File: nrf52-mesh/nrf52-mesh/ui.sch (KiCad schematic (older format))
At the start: 3 parts

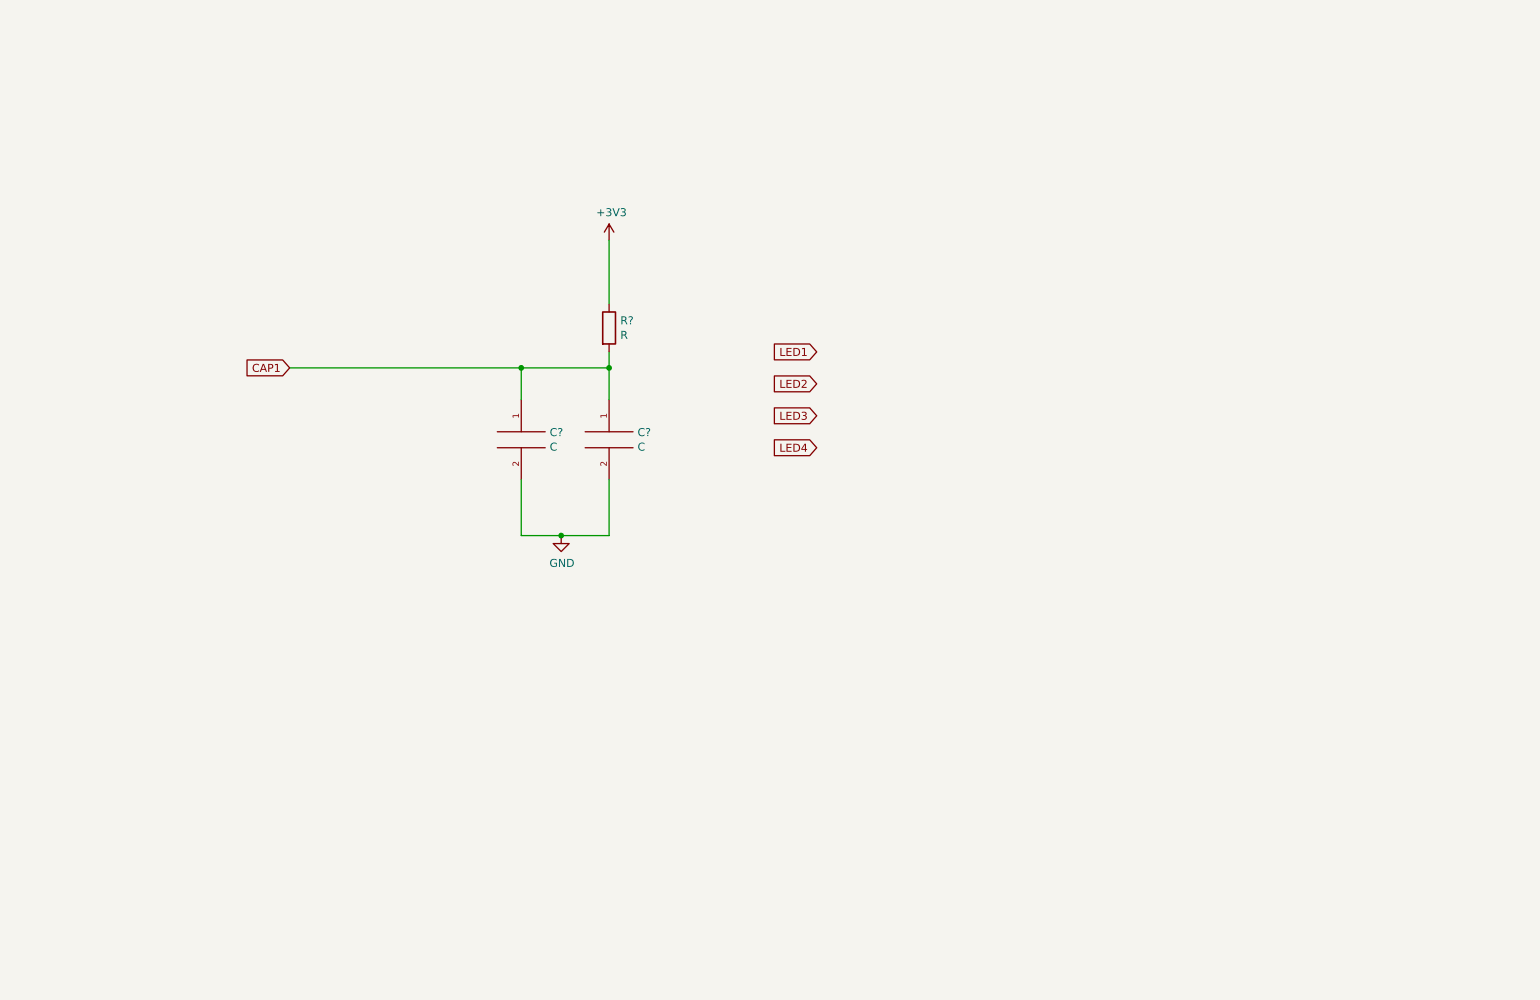
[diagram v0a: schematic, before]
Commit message: CP2102N + MAX1555 + FAN5341 + TPS560200 + TLV62568
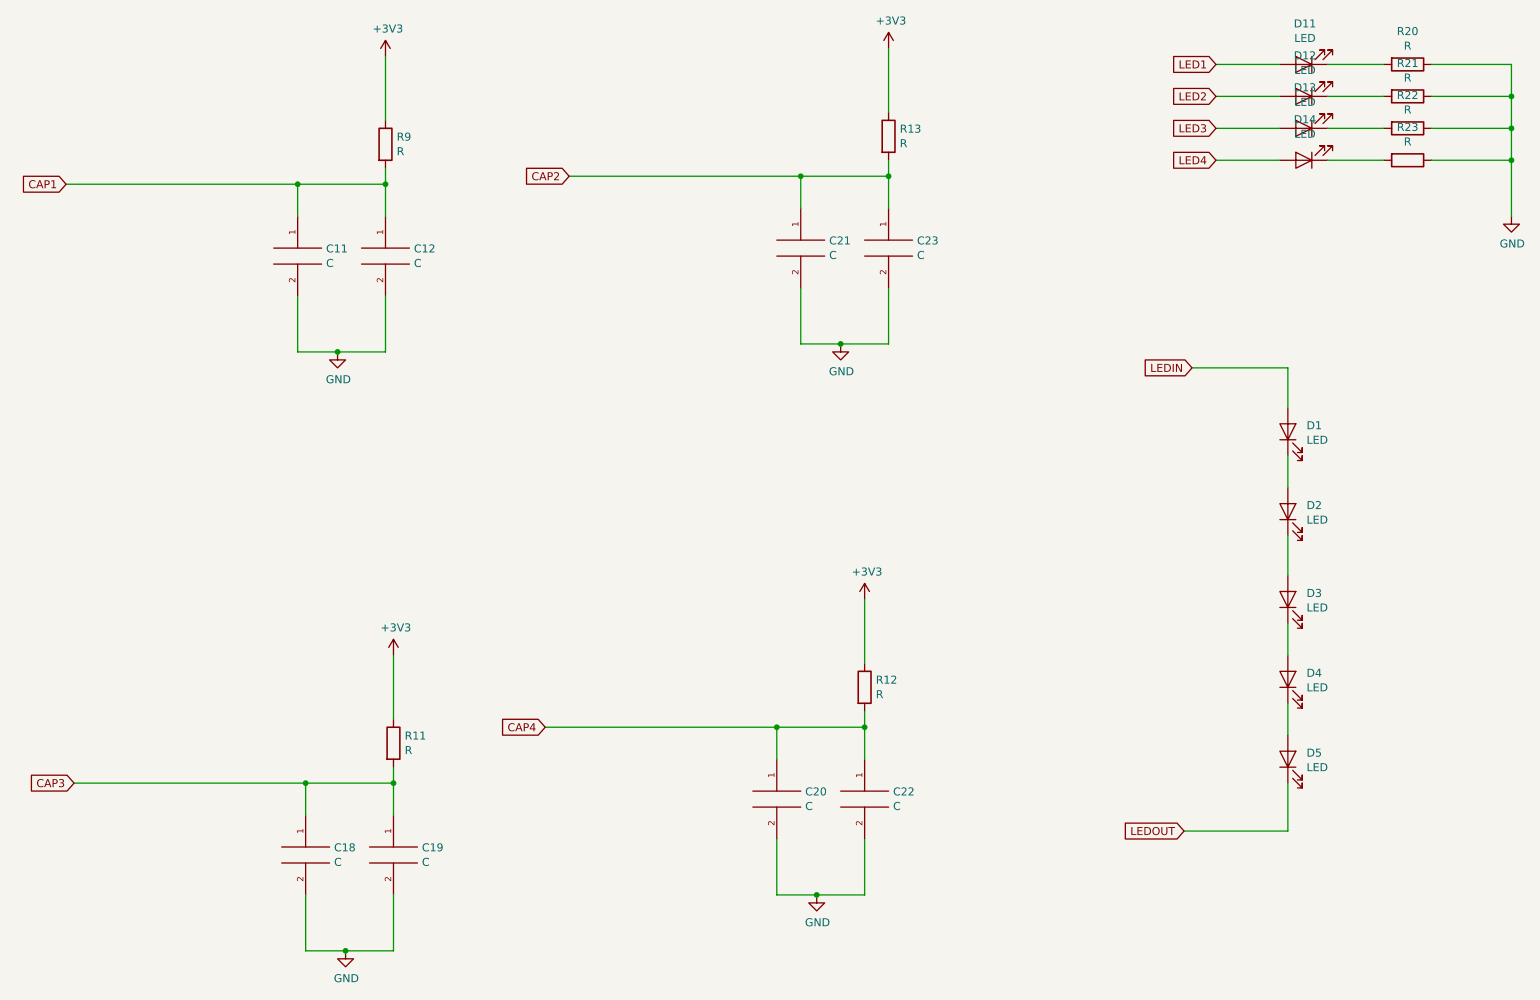
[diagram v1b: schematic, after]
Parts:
- added C18, C19, C20, C21, C22, C23: C, symbol pspice:C
- added D1, D11, D12, D13, D14, D2, D3, D4, D5: LED, symbol Device:LED
- added R11, R12, R13, R20, R21, R22, R23: R, symbol Device:R
- gave numbers to parts that had none: 3
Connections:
- net +3V3: now also R11.1, R12.1, R13.1
- net GND: now also C18.2, C19.2, C20.2, C21.2, C22.2, C23.2, R20.1, R21.1, R22.1, R23.1
- net LED1: now also D11.2 (A)
- net LED2: now also D12.2 (A)
- net LED3: now also D13.2 (A)
- net LED4: now also D14.2 (A)
- new net: D11.1 (K), R20.2
- new net: D12.1 (K), R21.2
- new net: D13.1 (K), R22.2
- new net: D14.1 (K), R23.2
- new net: D2.1 (K), D3.2 (A)
- new net: D1.1 (K), D2.2 (A)
- new net: D3.1 (K), D4.2 (A)
- new net: D4.1 (K), D5.2 (A)
- new net CAP2: C21.1, C23.1, R13.2
- new net CAP3: C18.1, C19.1, R11.2
- new net CAP4: C20.1, C22.1, R12.2
- new net LEDIN: D1.2 (A)
- new net LEDOUT: D5.1 (K)
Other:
- moved on the sheet: C11, C12, R9

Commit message: CP2102N + MAX1555 + FAN5341 + TPS560200 + TLV62568
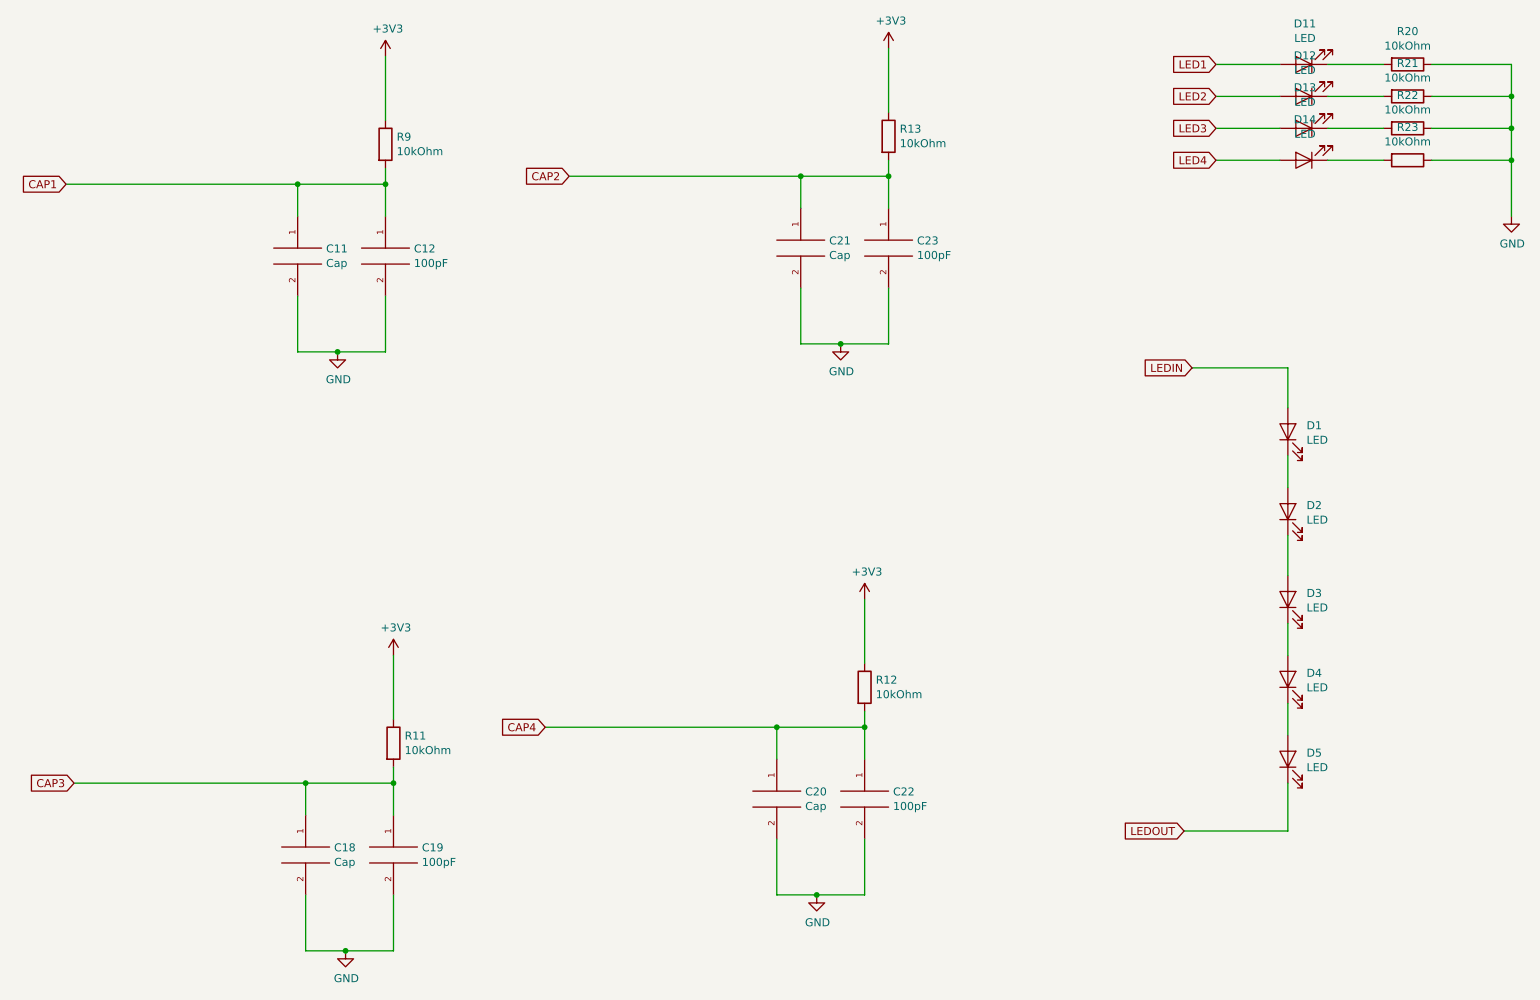
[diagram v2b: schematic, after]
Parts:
- C11, C18, C20, C21: value C -> Cap; footprint (none) -> kifootp:CAPBUTTON
- C12, C19, C22, C23: value C -> 100pF; footprint (none) -> Capacitor_SMD:C_0402_1005Metric
- D1, D11, D12, D13, D14, D2, D3, D4, D5: footprint (none) -> LED_SMD:LED_1206_3216Metric
- R11, R12, R13, R20, R21, R22, R23, R9: value R -> 10kOhm; footprint (none) -> Resistor_SMD:R_0402_1005Metric
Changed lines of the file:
@@
 P 3250 2400
 F 0 "C12" H 3428 2446 50  0000 L CNN
-F 1 "C" H 3428 2355 50  0000 L CNN
-F 2 "" H 3250 2400 50  0001 C CNN
+F 1 "100pF" H 3428 2355 50  0000 L CNN
+F 2 "Capacitor_SMD:C_0402_1005Metric" H 3250 2400 50  0001 C CNN
 F 3 "~" H 3250 2400 50  0001 C CNN
 	1    3250 2400
@@
 P 2700 2400
 F 0 "C11" H 2878 2446 50  0000 L CNN
-F 1 "C" H 2878 2355 50  0000 L CNN
-F 2 "" H 2700 2400 50  0001 C CNN
+F 1 "Cap" H 2878 2355 50  0000 L CNN
+F 2 "kifootp:CAPBUTTON" H 2700 2400 50  0001 C CNN
 F 3 "~" H 2700 2400 50  0001 C CNN
 	1    2700 2400
@@
 P 3250 1700
 F 0 "R9" H 3320 1746 50  0000 L CNN
-F 1 "R" H 3320 1655 50  0000 L CNN
-F 2 "" V 3180 1700 50  0001 C CNN
+F 1 "10kOhm" H 3320 1655 50  0000 L CNN
+F 2 "Resistor_SMD:R_0402_1005Metric" V 3180 1700 50  0001 C CNN
 F 3 "~" H 3250 1700 50  0001 C CNN
 	1    3250 1700
@@
 F 0 "D11" H 8993 945 50  0000 C CNN
 F 1 "LED" H 8993 1036 50  0000 C CNN
-F 2 "" H 9000 1200 50  0001 C CNN
+F 2 "LED_SMD:LED_1206_3216Metric" H 9000 1200 50  0001 C CNN
 F 3 "~" H 9000 1200 50  0001 C CNN
 	1    9000 1200
@@
 F 0 "D12" H 8993 1145 50  0000 C CNN
 F 1 "LED" H 8993 1236 50  0000 C CNN
-F 2 "" H 9000 1400 50  0001 C CNN
+F 2 "LED_SMD:LED_1206_3216Metric" H 9000 1400 50  0001 C CNN
 F 3 "~" H 9000 1400 50  0001 C CNN
 	1    9000 1400
@@
 F 0 "D13" H 8993 1345 50  0000 C CNN
 F 1 "LED" H 8993 1436 50  0000 C CNN
-F 2 "" H 9000 1600 50  0001 C CNN
+F 2 "LED_SMD:LED_1206_3216Metric" H 9000 1600 50  0001 C CNN
 F 3 "~" H 9000 1600 50  0001 C CNN
 	1    9000 1600
@@
 F 0 "D14" H 8993 1545 50  0000 C CNN
 F 1 "LED" H 8993 1636 50  0000 C CNN
-F 2 "" H 9000 1800 50  0001 C CNN
+F 2 "LED_SMD:LED_1206_3216Metric" H 9000 1800 50  0001 C CNN
 F 3 "~" H 9000 1800 50  0001 C CNN
 	1    9000 1800
@@
 P 9650 1200
 F 0 "R20" V 9443 1200 50  0000 C CNN
-F 1 "R" V 9534 1200 50  0000 C CNN
-F 2 "" V 9580 1200 50  0001 C CNN
+F 1 "10kOhm" V 9534 1200 50  0000 C CNN
+F 2 "Resistor_SMD:R_0402_1005Metric" V 9580 1200 50  0001 C CNN
 F 3 "~" H 9650 1200 50  0001 C CNN
 	1    9650 1200
@@
 P 9650 1400
 F 0 "R21" V 9443 1400 50  0000 C CNN
-F 1 "R" V 9534 1400 50  0000 C CNN
-F 2 "" V 9580 1400 50  0001 C CNN
+F 1 "10kOhm" V 9534 1400 50  0000 C CNN
+F 2 "Resistor_SMD:R_0402_1005Metric" V 9580 1400 50  0001 C CNN
 F 3 "~" H 9650 1400 50  0001 C CNN
 	1    9650 1400
@@
 P 9650 1600
 F 0 "R22" V 9443 1600 50  0000 C CNN
-F 1 "R" V 9534 1600 50  0000 C CNN
-F 2 "" V 9580 1600 50  0001 C CNN
+F 1 "10kOhm" V 9534 1600 50  0000 C CNN
+F 2 "Resistor_SMD:R_0402_1005Metric" V 9580 1600 50  0001 C CNN
 F 3 "~" H 9650 1600 50  0001 C CNN
 	1    9650 1600
@@
 P 9650 1800
 F 0 "R23" V 9443 1800 50  0000 C CNN
-F 1 "R" V 9534 1800 50  0000 C CNN
-F 2 "" V 9580 1800 50  0001 C CNN
+F 1 "10kOhm" V 9534 1800 50  0000 C CNN
+F 2 "Resistor_SMD:R_0402_1005Metric" V 9580 1800 50  0001 C CNN
 F 3 "~" H 9650 1800 50  0001 C CNN
 	1    9650 1800
@@
 P 3300 6150
 F 0 "C19" H 3478 6196 50  0000 L CNN
-F 1 "C" H 3478 6105 50  0000 L CNN
-F 2 "" H 3300 6150 50  0001 C CNN
+F 1 "100pF" H 3478 6105 50  0000 L CNN
+F 2 "Capacitor_SMD:C_0402_1005Metric" H 3300 6150 50  0001 C CNN
 F 3 "~" H 3300 6150 50  0001 C CNN
 	1    3300 6150
@@
 P 2750 6150
 F 0 "C18" H 2928 6196 50  0000 L CNN
-F 1 "C" H 2928 6105 50  0000 L CNN
-F 2 "" H 2750 6150 50  0001 C CNN
+F 1 "Cap" H 2928 6105 50  0000 L CNN
+F 2 "kifootp:CAPBUTTON" H 2750 6150 50  0001 C CNN
 F 3 "~" H 2750 6150 50  0001 C CNN
 	1    2750 6150
@@
 P 3300 5450
 F 0 "R11" H 3370 5496 50  0000 L CNN
-F 1 "R" H 3370 5405 50  0000 L CNN
-F 2 "" V 3230 5450 50  0001 C CNN
+F 1 "10kOhm" H 3370 5405 50  0000 L CNN
+F 2 "Resistor_SMD:R_0402_1005Metric" V 3230 5450 50  0001 C CNN
 F 3 "~" H 3300 5450 50  0001 C CNN
 	1    3300 5450
@@
 P 6400 2350
 F 0 "C23" H 6578 2396 50  0000 L CNN
-F 1 "C" H 6578 2305 50  0000 L CNN
-F 2 "" H 6400 2350 50  0001 C CNN
+F 1 "100pF" H 6578 2305 50  0000 L CNN
+F 2 "Capacitor_SMD:C_0402_1005Metric" H 6400 2350 50  0001 C CNN
 F 3 "~" H 6400 2350 50  0001 C CNN
 	1    6400 2350
@@
 P 5850 2350
 F 0 "C21" H 6028 2396 50  0000 L CNN
-F 1 "C" H 6028 2305 50  0000 L CNN
-F 2 "" H 5850 2350 50  0001 C CNN
+F 1 "Cap" H 6028 2305 50  0000 L CNN
+F 2 "kifootp:CAPBUTTON" H 5850 2350 50  0001 C CNN
 F 3 "~" H 5850 2350 50  0001 C CNN
 	1    5850 2350
@@
 P 6400 1650
 F 0 "R13" H 6470 1696 50  0000 L CNN
-F 1 "R" H 6470 1605 50  0000 L CNN
-F 2 "" V 6330 1650 50  0001 C CNN
+F 1 "10kOhm" H 6470 1605 50  0000 L CNN
+F 2 "Resistor_SMD:R_0402_1005Metric" V 6330 1650 50  0001 C CNN
 F 3 "~" H 6400 1650 50  0001 C CNN
 	1    6400 1650
@@
 P 6250 5800
 F 0 "C22" H 6428 5846 50  0000 L CNN
-F 1 "C" H 6428 5755 50  0000 L CNN
-F 2 "" H 6250 5800 50  0001 C CNN
+F 1 "100pF" H 6428 5755 50  0000 L CNN
+F 2 "Capacitor_SMD:C_0402_1005Metric" H 6250 5800 50  0001 C CNN
 F 3 "~" H 6250 5800 50  0001 C CNN
 	1    6250 5800
@@
 P 5700 5800
 F 0 "C20" H 5878 5846 50  0000 L CNN
-F 1 "C" H 5878 5755 50  0000 L CNN
-F 2 "" H 5700 5800 50  0001 C CNN
+F 1 "Cap" H 5878 5755 50  0000 L CNN
+F 2 "kifootp:CAPBUTTON" H 5700 5800 50  0001 C CNN
 F 3 "~" H 5700 5800 50  0001 C CNN
 	1    5700 5800
@@
 P 6250 5100
 F 0 "R12" H 6320 5146 50  0000 L CNN
-F 1 "R" H 6320 5055 50  0000 L CNN
-F 2 "" V 6180 5100 50  0001 C CNN
+F 1 "10kOhm" H 6320 5055 50  0000 L CNN
+F 2 "Resistor_SMD:R_0402_1005Metric" V 6180 5100 50  0001 C CNN
 F 3 "~" H 6250 5100 50  0001 C CNN
 	1    6250 5100
@@
 F 0 "D2" V 8939 3883 50  0000 R CNN
 F 1 "LED" V 8848 3883 50  0000 R CNN
-F 2 "" H 8900 4000 50  0001 C CNN
+F 2 "LED_SMD:LED_1206_3216Metric" H 8900 4000 50  0001 C CNN
 F 3 "~" H 8900 4000 50  0001 C CNN
 	1    8900 4000
@@
 F 0 "D3" V 8939 4433 50  0000 R CNN
 F 1 "LED" V 8848 4433 50  0000 R CNN
-F 2 "" H 8900 4550 50  0001 C CNN
+F 2 "LED_SMD:LED_1206_3216Metric" H 8900 4550 50  0001 C CNN
 F 3 "~" H 8900 4550 50  0001 C CNN
 	1    8900 4550
@@
 F 0 "D1" V 8939 3383 50  0000 R CNN
 F 1 "LED" V 8848 3383 50  0000 R CNN
-F 2 "" H 8900 3500 50  0001 C CNN
+F 2 "LED_SMD:LED_1206_3216Metric" H 8900 3500 50  0001 C CNN
 F 3 "~" H 8900 3500 50  0001 C CNN
 	1    8900 3500
@@
 F 0 "D4" V 8939 4933 50  0000 R CNN
 F 1 "LED" V 8848 4933 50  0000 R CNN
-F 2 "" H 8900 5050 50  0001 C CNN
+F 2 "LED_SMD:LED_1206_3216Metric" H 8900 5050 50  0001 C CNN
 F 3 "~" H 8900 5050 50  0001 C CNN
 	1    8900 5050
@@
 F 0 "D5" V 8939 5433 50  0000 R CNN
 F 1 "LED" V 8848 5433 50  0000 R CNN
-F 2 "" H 8900 5550 50  0001 C CNN
+F 2 "LED_SMD:LED_1206_3216Metric" H 8900 5550 50  0001 C CNN
 F 3 "~" H 8900 5550 50  0001 C CNN
 	1    8900 5550

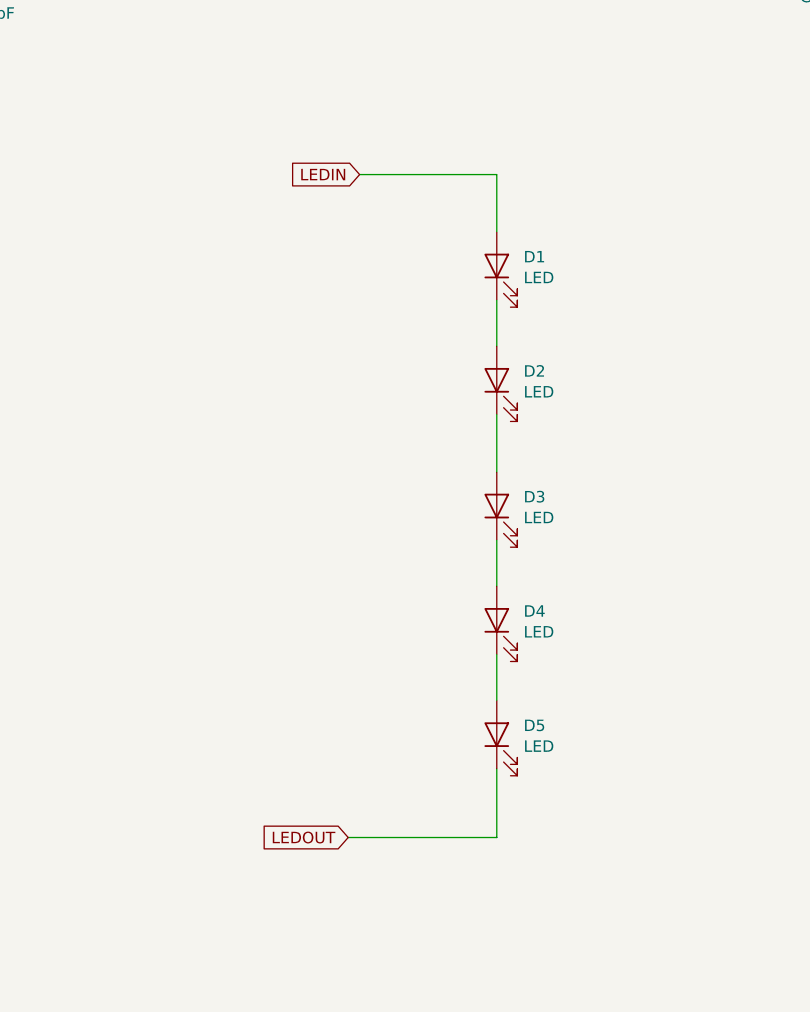
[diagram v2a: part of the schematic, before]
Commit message: nRF52 + ESP WROOM
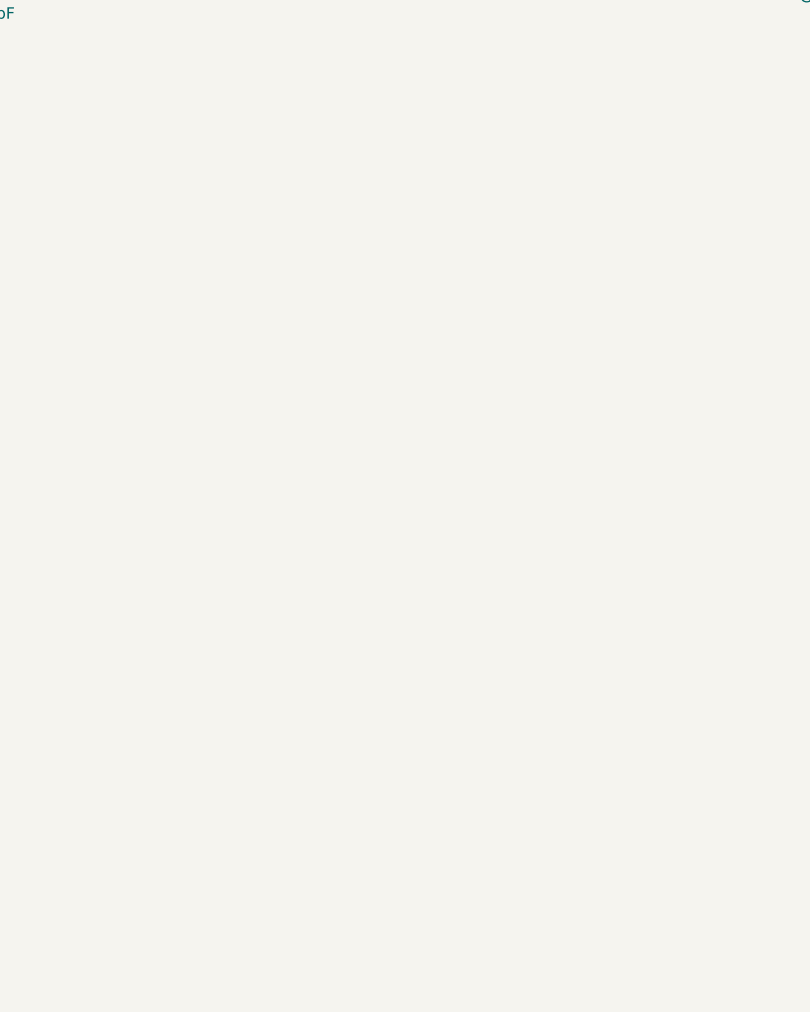
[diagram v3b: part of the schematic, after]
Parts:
- removed D1, D2, D3, D4, D5: LED, LED_SMD:LED_1206_3216Metric, symbol Device:LED
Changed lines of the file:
@@
 $Descr A4 11693 8268
 encoding utf-8
-Sheet 6 8
+Sheet 6 9
 Title ""
 Date ""
@@
 Text GLabel 4250 5350 0    50   Input ~ 0
 CAP4
-Text GLabel 8300 3100 0    50   Input ~ 0
-LEDIN
-Text GLabel 8250 6000 0    50   Input ~ 0
-LEDOUT
-$Comp
-L Device:LED D2
-U 1 1 5E6052AF
-P 8900 4000
-F 0 "D2" V 8939 3883 50  0000 R CNN
-F 1 "LED" V 8848 3883 50  0000 R CNN
-F 2 "LED_SMD:LED_1206_3216Metric" H 8900 4000 50  0001 C CNN
-F 3 "~" H 8900 4000 50  0001 C CNN
-	1    8900 4000
-	0    -1   -1   0
-$EndComp
-$Comp
-L Device:LED D3
-U 1 1 5E607081
-P 8900 4550
-F 0 "D3" V 8939 4433 50  0000 R CNN
-F 1 "LED" V 8848 4433 50  0000 R CNN
-F 2 "LED_SMD:LED_1206_3216Metric" H 8900 4550 50  0001 C CNN
-F 3 "~" H 8900 4550 50  0001 C CNN
-	1    8900 4550
-	0    -1   -1   0
-$EndComp
-$Comp
-L Device:LED D1
-U 1 1 5E608150
-P 8900 3500
-F 0 "D1" V 8939 3383 50  0000 R CNN
-F 1 "LED" V 8848 3383 50  0000 R CNN
-F 2 "LED_SMD:LED_1206_3216Metric" H 8900 3500 50  0001 C CNN
-F 3 "~" H 8900 3500 50  0001 C CNN
-	1    8900 3500
-	0    -1   -1   0
-$EndComp
-$Comp
-L Device:LED D4
-U 1 1 5E60928F
-P 8900 5050
-F 0 "D4" V 8939 4933 50  0000 R CNN
-F 1 "LED" V 8848 4933 50  0000 R CNN
-F 2 "LED_SMD:LED_1206_3216Metric" H 8900 5050 50  0001 C CNN
-F 3 "~" H 8900 5050 50  0001 C CNN
-	1    8900 5050
-	0    -1   -1   0
-$EndComp
-$Comp
-L Device:LED D5
-U 1 1 5E60A404
-P 8900 5550
-F 0 "D5" V 8939 5433 50  0000 R CNN
-F 1 "LED" V 8848 5433 50  0000 R CNN
-F 2 "LED_SMD:LED_1206_3216Metric" H 8900 5550 50  0001 C CNN
-F 3 "~" H 8900 5550 50  0001 C CNN
-	1    8900 5550
-	0    -1   -1   0
-$EndComp
-Wire Wire Line
-	8300 3100 8900 3100
-Wire Wire Line
-	8900 3100 8900 3350
-Wire Wire Line
-	8900 3650 8900 3850
-Wire Wire Line
-	8900 4150 8900 4400
-Wire Wire Line
-	8900 4700 8900 4900
-Wire Wire Line
-	8900 5200 8900 5400
-Wire Wire Line
-	8900 5700 8900 6000
-Wire Wire Line
-	8900 6000 8250 6000
 $EndSCHEMATC
